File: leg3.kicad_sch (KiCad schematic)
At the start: 12 parts, among them J10 Leg3 Motor3, J8 Leg3 Motor1, J9 Leg3 Motor2

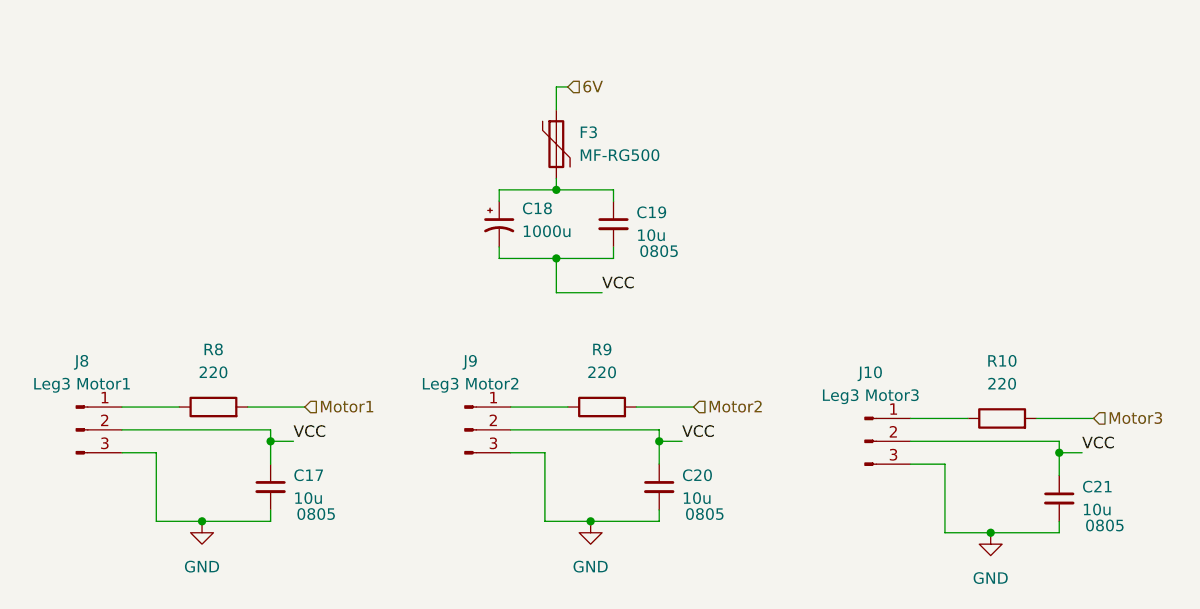
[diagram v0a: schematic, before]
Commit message: removed crystal, fixed caps
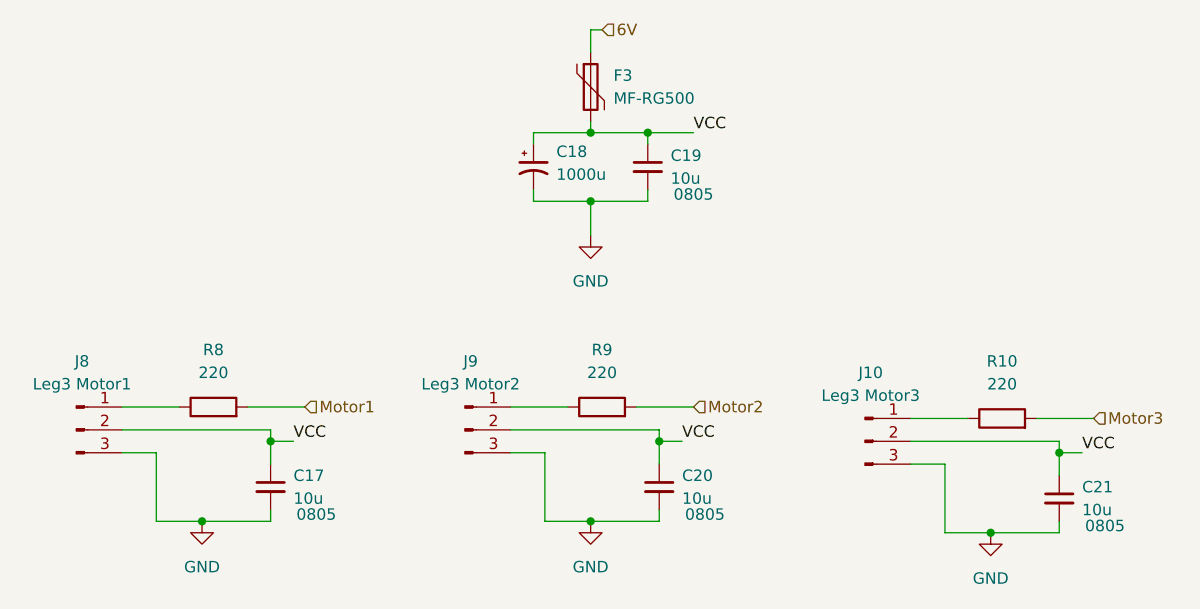
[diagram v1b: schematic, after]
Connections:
- net GND: now also C18.2, C19.2
- net VCC: now also C18.1, C19.1, F3.2; no longer C18.2, C19.2
